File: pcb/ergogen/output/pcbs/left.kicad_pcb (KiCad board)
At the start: 2 copper layers, 143.3 x 86.2 mm, 54 parts

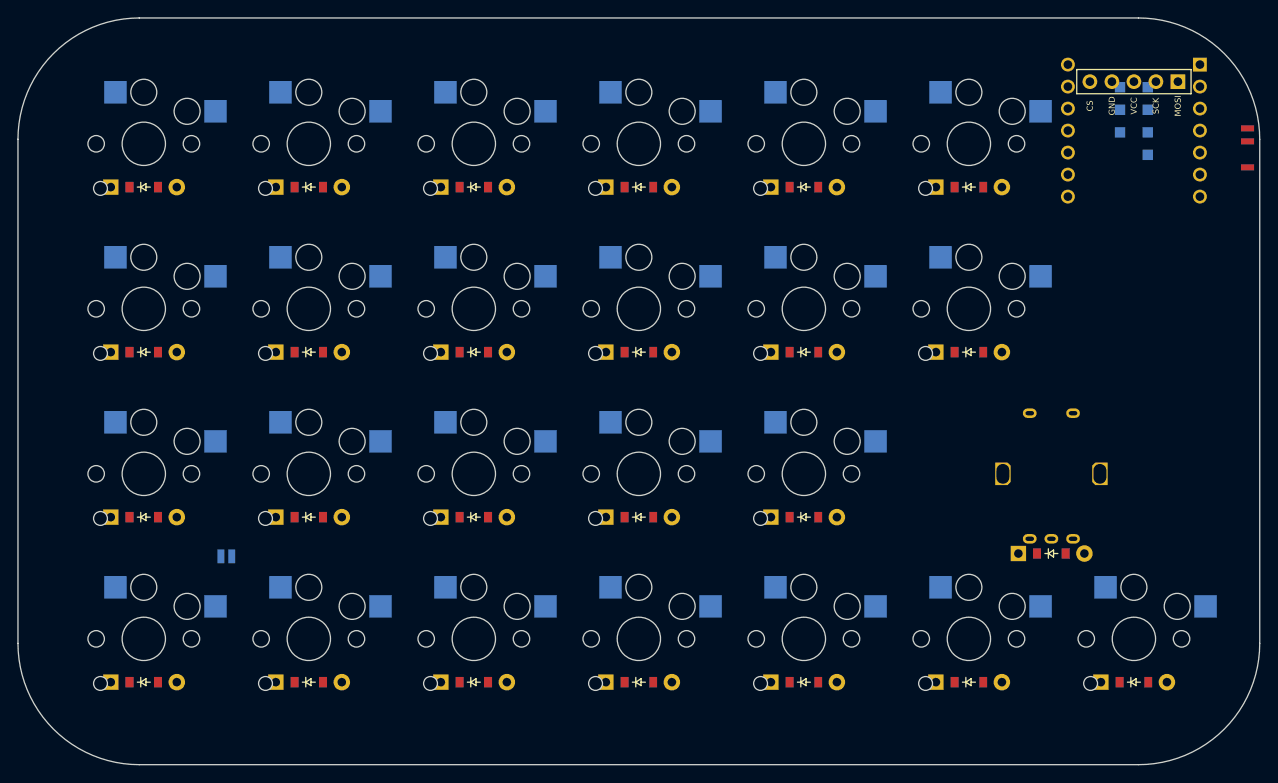
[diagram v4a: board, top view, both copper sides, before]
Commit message: Gasket-mount PCB/plate outlines and 3D-printable case
- Ergogen: cavity/top-opening outlines, plate with 6 gasket tabs,
  PCB 0.75mm inside the case with tongues for USB-C and power switch
- XIAO turned sideways so USB-C exits the inner side wall
- case/kataware_case.py builds top and bottom case STLs from the DXFs
- Section drawings, 3D renders and README/KiCad guide updates

Co-Authored-By: Claude Opus 5.5 <noreply@anthropic.com>
Claude-Session: https://claude.ai/code/session_017zNm7dMSTHELcztuNr6aNy
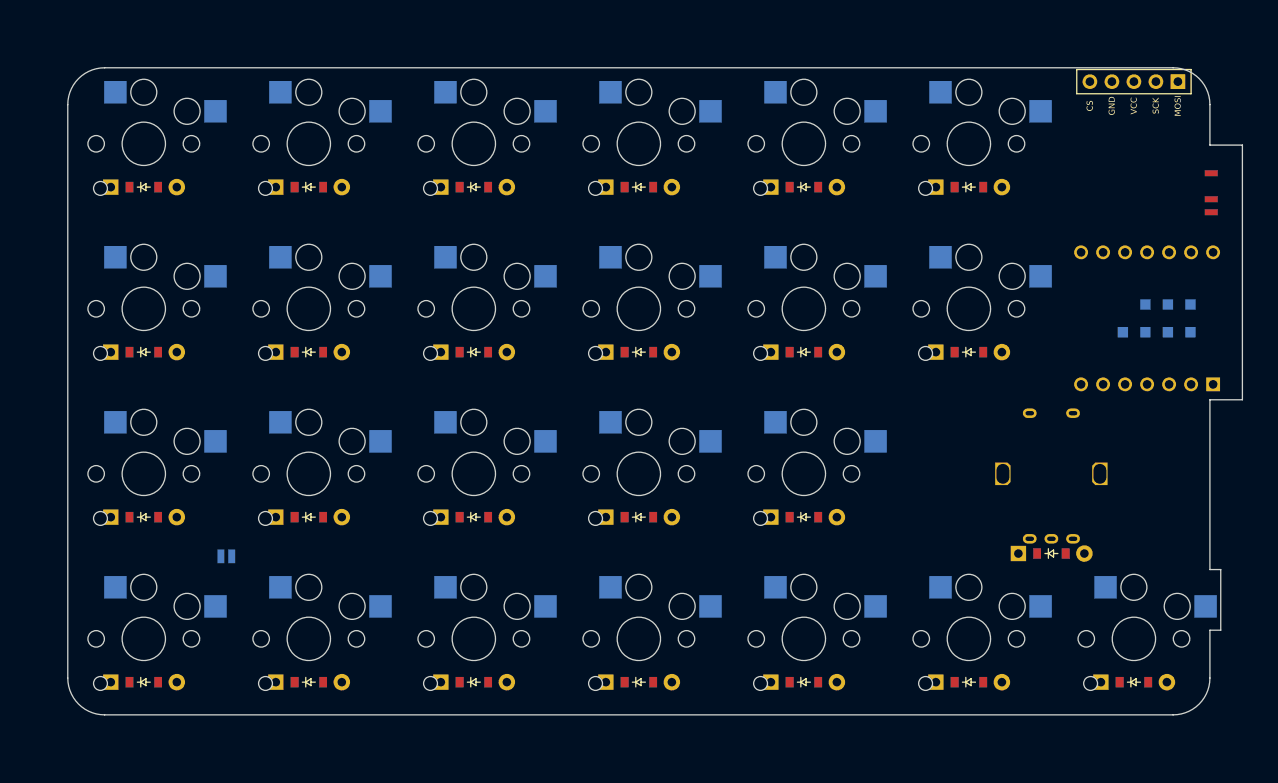
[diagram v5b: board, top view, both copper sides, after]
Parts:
- moved MCU1 21.7 mm to (115.8, -37.0), turned to -90 degrees
- moved PWR1 5.17 mm to (125.3, -51.5), turned to -90 degrees
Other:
- board size 143.3 x 86.2 mm -> 135.6 x 74.7 mm

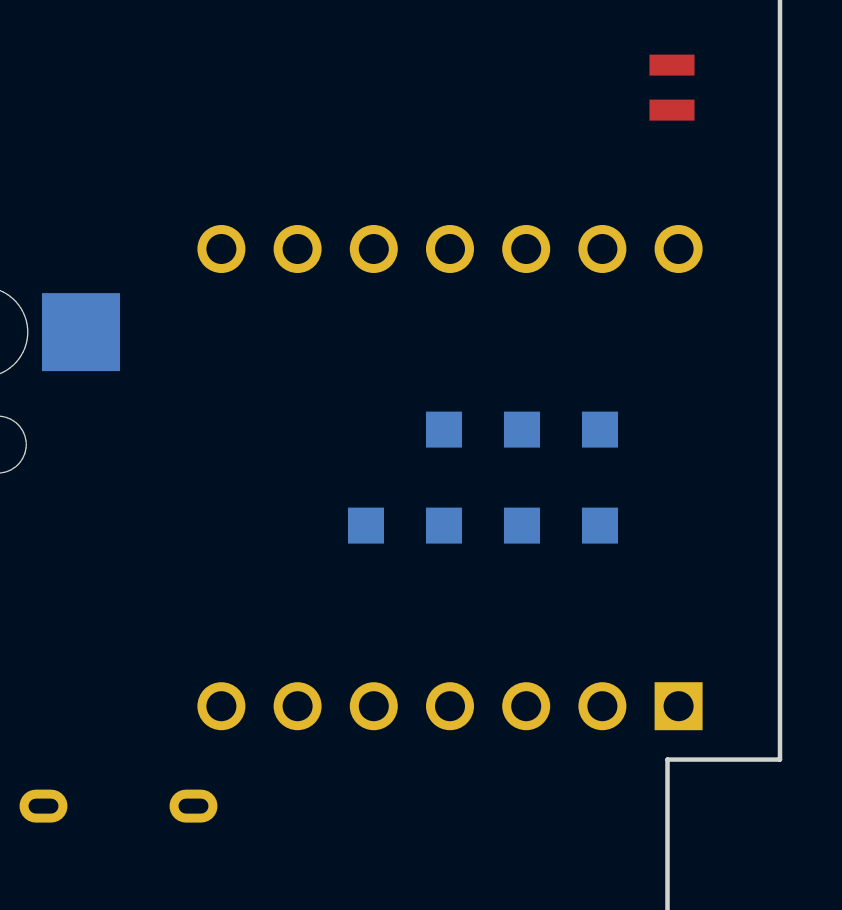
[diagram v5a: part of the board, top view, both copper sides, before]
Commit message: Move the trackball under the [ ] column at the N row
- Ball centre to (-8, 11) from the e column / thumb row: the cover now
  ends ~1mm below the ] keycap and ~1mm from N/Enter (the limit)
- The unit now sits inside the case cavity, so the right case wall
  bulge is gone and both halves share the same cavity
- XIAO raised 1.5mm to clear the ball hole; sensor cable moves to a
  JST SH 6-pin SMD connector (J) on the back between Enter and N, and
  the base cable exit faces it
- Fix draw_case_section so the thumb/tab/USB sections are written again
- README, KiCad guide, template and images updated

Co-Authored-By: Claude Opus 5.5 <noreply@anthropic.com>
Claude-Session: https://claude.ai/code/session_017zNm7dMSTHELcztuNr6aNy
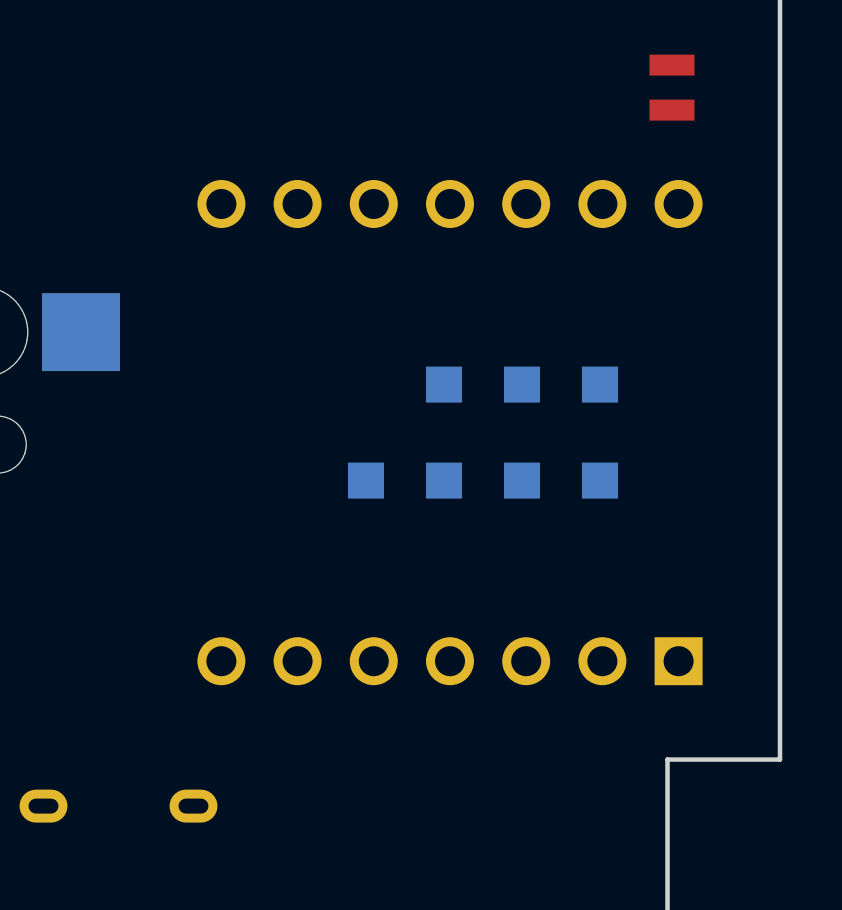
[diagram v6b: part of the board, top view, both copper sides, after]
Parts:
- moved MCU1 1.50 mm to (115.8, -38.5)
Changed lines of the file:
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@@
   (title_block
     (title "left")
-    (date "2026-10-16")
+    (date "2026-10-17")
     (rev "0.1")
     (company "kyonccc")
@@
     )
       (module kataware_xiao_plus_placeholder (layer B.Cu)
-      (at 115.825 -37 -90)
+      (at 115.825 -38.5 -90)
       (fp_text reference "MCU1" (at 0 -12) (layer B.SilkS) hide (effects (font (size 1 1) (thickness 0.15)) (justify mirror)))
       (fp_text value "" (at 0 0) (layer B.SilkS) hide (effects (font (size 1 1) (thickness 0.15)) (justify mirror)))
